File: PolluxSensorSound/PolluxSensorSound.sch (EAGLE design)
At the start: 5 parts

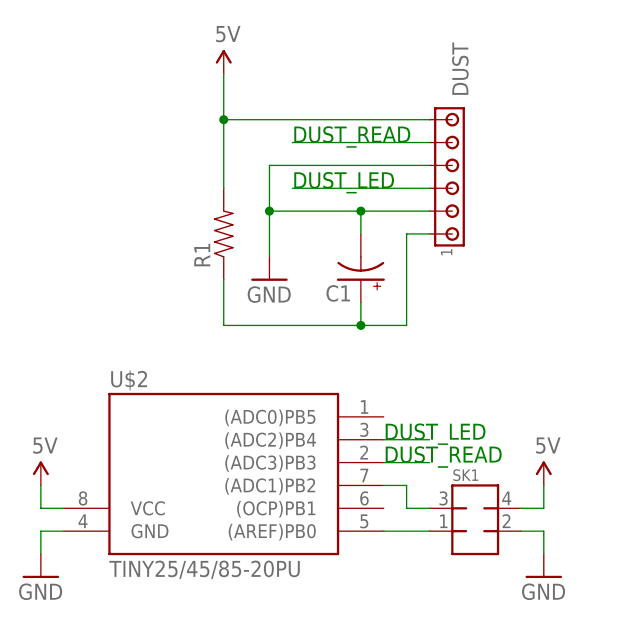
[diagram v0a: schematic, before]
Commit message: add SPL sensor board and schematics
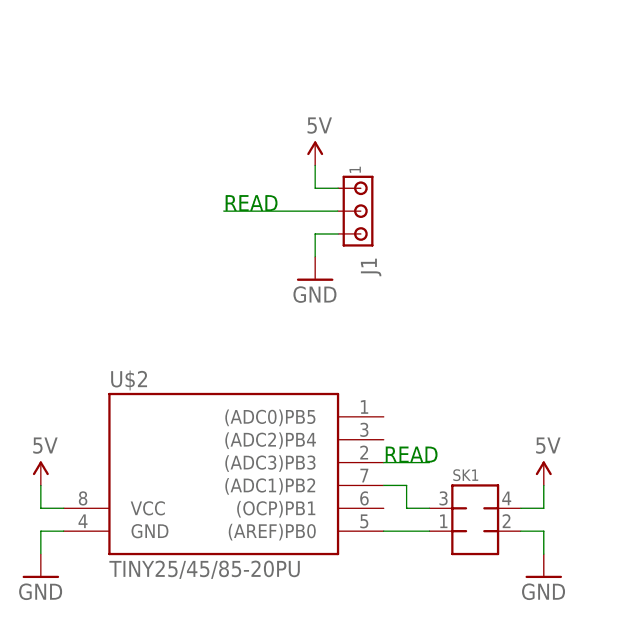
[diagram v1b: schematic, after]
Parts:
- removed C1: (no value), SparkFun:CAP_POLPTH4
- removed DUST: (no value), con-amp:MTA06-100
- removed R1: (no value), SparkFun:RESISTORAXIAL-0.3
- added J1: (no value), con-amp:MTA03-100
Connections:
- removed net DUST_LED: DUST.3, U$2.(ADC2)PB4
- removed net DUST_READ: DUST.5, U$2.(ADC3)PB3
- removed net N$4: C1.+, DUST.1, R1.1
- new net READ: J1.2, U$2.(ADC3)PB3
- net 5V: now also J1.1; no longer DUST.6, R1.2
- net GND: now also J1.3; no longer C1.-, DUST.2, DUST.4
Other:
- note added: "READ"
- note removed: "DUST_LED"
- note removed: "DUST_READ"
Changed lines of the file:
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@@
 <part name="SK1" library="jt-con-micromatch" deviceset="MMATCH-8-*" device="PTH"/>
 <part name="U$2" library="avr-7" deviceset="TINY25/45/85" device="-20PU"/>
-<part name="C1" library="SparkFun" deviceset="CAP_POL" device="PTH4"/>
-<part name="R1" library="SparkFun" deviceset="RESISTOR" device="AXIAL-0.3"/>
-<part name="DUST" library="con-amp" deviceset="MTA06-100" device=""/>
 <part name="U$3" library="SparkFun" deviceset="5V" device=""/>
 <part name="U$4" library="SparkFun" deviceset="5V" device=""/>
 <part name="GND2" library="SparkFun" deviceset="GND" device=""/>
 <part name="GND3" library="SparkFun" deviceset="GND" device=""/>
+<part name="J1" library="con-amp" deviceset="MTA03-100" device=""/>
 </parts>
 <sheets>
 <sheet>
 <plain>
-<text x="71.12" y="30.48" size="1.778" layer="91">DUST_READ</text>
-<text x="71.12" y="33.02" size="1.778" layer="91">DUST_LED</text>
-<text x="60.96" y="60.96" size="1.778" layer="91">DUST_LED</text>
-<text x="60.96" y="66.04" size="1.778" layer="91">DUST_READ</text>
+<text x="71.12" y="30.48" size="1.778" layer="91">READ</text>
+<text x="53.34" y="58.42" size="1.778" layer="91">READ</text>
 </plain>
 <instances>
-<instance part="U$1" gate="G$1" x="53.34" y="73.66"/>
+<instance part="U$1" gate="G$1" x="63.5" y="63.5"/>
 <instance part="GND1" gate="1" x="88.9" y="17.78"/>
 <instance part="SK1" gate="G$1" x="81.28" y="22.86"/>
 <instance part="U$2" gate="G$1" x="53.34" y="27.94"/>
-<instance part="C1" gate="G$1" x="68.58" y="50.8" rot="R180"/>
-<instance part="R1" gate="G$1" x="53.34" y="55.88" rot="R90"/>
-<instance part="DUST" gate="G$1" x="78.74" y="60.96" rot="MR90"/>
 <instance part="U$3" gate="G$1" x="33.02" y="27.94"/>
 <instance part="U$4" gate="G$1" x="88.9" y="27.94"/>
 <instance part="GND2" gate="1" x="33.02" y="17.78"/>
-<instance part="GND3" gate="1" x="58.42" y="50.8"/>
+<instance part="GND3" gate="1" x="63.5" y="50.8"/>
+<instance part="J1" gate="G$1" x="68.58" y="58.42" rot="R270"/>
 </instances>
 <busses>
@@
 </segment>
 <segment>
-<pinref part="R1" gate="G$1" pin="2"/>
+<pinref part="J1" gate="G$1" pin="1"/>
 <pinref part="U$1" gate="G$1" pin="5V"/>
-<wire x1="53.34" y1="60.96" x2="53.34" y2="68.58" width="0.1524" layer="91"/>
-<wire x1="53.34" y1="68.58" x2="53.34" y2="73.66" width="0.1524" layer="91"/>
-<wire x1="53.34" y1="68.58" x2="76.2" y2="68.58" width="0.1524" layer="91"/>
-<pinref part="DUST" gate="G$1" pin="6"/>
-<junction x="53.34" y="68.58"/>
-</segment>
-</net>
-<net name="DUST_LED" class="0">
-<segment>
-<pinref part="DUST" gate="G$1" pin="3"/>
-<wire x1="76.2" y1="60.96" x2="60.96" y2="60.96" width="0.1524" layer="91"/>
-</segment>
-<segment>
-<pinref part="U$2" gate="G$1" pin="(ADC2)PB4"/>
-<wire x1="71.12" y1="33.02" x2="76.2" y2="33.02" width="0.1524" layer="91"/>
+<wire x1="66.04" y1="60.96" x2="63.5" y2="60.96" width="0.1524" layer="91"/>
+<wire x1="63.5" y1="60.96" x2="63.5" y2="63.5" width="0.1524" layer="91"/>
 </segment>
 </net>
@@
 <segment>
 <pinref part="GND3" gate="1" pin="GND"/>
-<wire x1="58.42" y1="53.34" x2="58.42" y2="58.42" width="0.1524" layer="91"/>
-<pinref part="DUST" gate="G$1" pin="2"/>
-<wire x1="76.2" y1="58.42" x2="68.58" y2="58.42" width="0.1524" layer="91"/>
-<pinref part="C1" gate="G$1" pin="-"/>
-<wire x1="68.58" y1="58.42" x2="68.58" y2="55.88" width="0.1524" layer="91"/>
-<wire x1="58.42" y1="58.42" x2="68.58" y2="58.42" width="0.1524" layer="91"/>
-<wire x1="58.42" y1="58.42" x2="58.42" y2="63.5" width="0.1524" layer="91"/>
-<pinref part="DUST" gate="G$1" pin="4"/>
-<wire x1="58.42" y1="63.5" x2="76.2" y2="63.5" width="0.1524" layer="91"/>
-<junction x="58.42" y="58.42"/>
-<junction x="68.58" y="58.42"/>
+<wire x1="63.5" y1="53.34" x2="63.5" y2="55.88" width="0.1524" layer="91"/>
+<pinref part="J1" gate="G$1" pin="3"/>
+<wire x1="63.5" y1="55.88" x2="66.04" y2="55.88" width="0.1524" layer="91"/>
 </segment>
 </net>
@@
 </segment>
 </net>
-<net name="DUST_READ" class="0">
+<net name="READ" class="0">
 <segment>
-<pinref part="DUST" gate="G$1" pin="5"/>
-<wire x1="76.2" y1="66.04" x2="60.96" y2="66.04" width="0.1524" layer="91"/>
+<pinref part="J1" gate="G$1" pin="2"/>
+<wire x1="66.04" y1="58.42" x2="53.34" y2="58.42" width="0.1524" layer="91"/>
 </segment>
 <segment>
@@
 </segment>
 </net>
-<net name="N$4" class="0">
-<segment>
-<pinref part="R1" gate="G$1" pin="1"/>
-<wire x1="53.34" y1="50.8" x2="53.34" y2="45.72" width="0.1524" layer="91"/>
-<pinref part="DUST" gate="G$1" pin="1"/>
-<wire x1="76.2" y1="55.88" x2="73.66" y2="55.88" width="0.1524" layer="91"/>
-<wire x1="73.66" y1="55.88" x2="73.66" y2="45.72" width="0.1524" layer="91"/>
-<wire x1="73.66" y1="45.72" x2="68.58" y2="45.72" width="0.1524" layer="91"/>
-<pinref part="C1" gate="G$1" pin="+"/>
-<wire x1="68.58" y1="45.72" x2="53.34" y2="45.72" width="0.1524" layer="91"/>
-<wire x1="68.58" y1="48.26" x2="68.58" y2="45.72" width="0.1524" layer="91"/>
-<junction x="68.58" y="45.72"/>
-</segment>
-</net>

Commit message: improve sensor board
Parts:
- removed J1: (no value), con-amp:MTA03-100
- added C1: 1 uF, SparkFun:CAP_POLPTH2
- added SOUND: (no value), pinhead-2:PINHD-1X04_2.00
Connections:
- removed net N$2 (its old number): SK1.1, U$2.(AREF)PB0
- new net SDA: SK1.4, U$2.(AREF)PB0
- net 5V: now also C1.+, SK1.1, SOUND.3; no longer J1.1, SK1.4
- net GND: now also C1.-, SOUND.4; no longer J1.3
- net READ: now also SOUND.1; no longer J1.2
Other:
- note added: "SCL"
- note added: "SDA"
- moved on the sheet: SK1
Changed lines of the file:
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@@
 <layer number="56" name="wert" color="7" fill="1" visible="no" active="no"/>
 <layer number="91" name="Nets" color="2" fill="1" visible="yes" active="yes"/>
-<layer number="92" name="Busses" color="1" fill="1" visible="yes" active="yes"/>
+<layer number="92" name="Busses" color="1" fill="1" visible="no" active="yes"/>
 <layer number="93" name="Pins" color="2" fill="1" visible="no" active="yes"/>
 <layer number="94" name="Symbols" color="4" fill="1" visible="yes" active="yes"/>
@@
 <part name="GND2" library="SparkFun" deviceset="GND" device=""/>
 <part name="GND3" library="SparkFun" deviceset="GND" device=""/>
-<part name="J1" library="con-amp" deviceset="MTA03-100" device=""/>
+<part name="C1" library="SparkFun" deviceset="CAP_POL" device="PTH2" value="1 uF"/>
+<part name="U$5" library="SparkFun" deviceset="5V" device=""/>
+<part name="GND4" library="SparkFun" deviceset="GND" device=""/>
+<part name="SOUND" library="pinhead-2" deviceset="PINHD-1X04" device="_2.00"/>
 </parts>
 <sheets>
@@
 <plain>
 <text x="71.12" y="30.48" size="1.778" layer="91">READ</text>
-<text x="53.34" y="58.42" size="1.778" layer="91">READ</text>
+<text x="60.96" y="60.96" size="1.778" layer="91">READ</text>
+<text x="71.12" y="22.86" size="1.778" layer="91">SDA</text>
+<text x="91.44" y="27.94" size="1.778" layer="91">SDA</text>
+<text x="71.12" y="27.94" size="1.778" layer="91">SCL</text>
 </plain>
 <instances>
-<instance part="U$1" gate="G$1" x="63.5" y="63.5"/>
-<instance part="GND1" gate="1" x="88.9" y="17.78"/>
-<instance part="SK1" gate="G$1" x="81.28" y="22.86"/>
+<instance part="U$1" gate="G$1" x="68.58" y="63.5"/>
+<instance part="GND1" gate="1" x="93.98" y="20.32"/>
+<instance part="SK1" gate="G$1" x="86.36" y="25.4"/>
 <instance part="U$2" gate="G$1" x="53.34" y="27.94"/>
-<instance part="U$3" gate="G$1" x="33.02" y="27.94"/>
-<instance part="U$4" gate="G$1" x="88.9" y="27.94"/>
+<instance part="U$3" gate="G$1" x="33.02" y="38.1"/>
+<instance part="U$4" gate="G$1" x="78.74" y="35.56"/>
 <instance part="GND2" gate="1" x="33.02" y="17.78"/>
-<instance part="GND3" gate="1" x="63.5" y="50.8"/>
-<instance part="J1" gate="G$1" x="68.58" y="58.42" rot="R270"/>
+<instance part="GND3" gate="1" x="68.58" y="48.26"/>
+<instance part="C1" gate="G$1" x="86.36" y="58.42"/>
+<instance part="U$5" gate="G$1" x="86.36" y="63.5"/>
+<instance part="GND4" gate="1" x="86.36" y="48.26"/>
+<instance part="SOUND" gate="A" x="78.74" y="55.88"/>
 </instances>
 <busses>
 </busses>
 <nets>
-<net name="N$2" class="0">
-<segment>
-<pinref part="SK1" gate="G$1" pin="1"/>
-<pinref part="U$2" gate="G$1" pin="(AREF)PB0"/>
-<wire x1="76.2" y1="22.86" x2="71.12" y2="22.86" width="0.1524" layer="91"/>
-</segment>
-</net>
 <net name="5V" class="0">
-<segment>
-<pinref part="SK1" gate="G$1" pin="4"/>
-<wire x1="86.36" y1="25.4" x2="88.9" y2="25.4" width="0.1524" layer="91"/>
-<pinref part="U$4" gate="G$1" pin="5V"/>
-<wire x1="88.9" y1="25.4" x2="88.9" y2="27.94" width="0.1524" layer="91"/>
-</segment>
 <segment>
 <pinref part="U$2" gate="G$1" pin="VCC"/>
 <wire x1="35.56" y1="25.4" x2="33.02" y2="25.4" width="0.1524" layer="91"/>
 <pinref part="U$3" gate="G$1" pin="5V"/>
-<wire x1="33.02" y1="25.4" x2="33.02" y2="27.94" width="0.1524" layer="91"/>
+<wire x1="33.02" y1="25.4" x2="33.02" y2="38.1" width="0.1524" layer="91"/>
 </segment>
 <segment>
-<pinref part="J1" gate="G$1" pin="1"/>
 <pinref part="U$1" gate="G$1" pin="5V"/>
-<wire x1="66.04" y1="60.96" x2="63.5" y2="60.96" width="0.1524" layer="91"/>
-<wire x1="63.5" y1="60.96" x2="63.5" y2="63.5" width="0.1524" layer="91"/>
+<wire x1="68.58" y1="55.88" x2="68.58" y2="63.5" width="0.1524" layer="91"/>
+<pinref part="SOUND" gate="A" pin="3"/>
+<wire x1="76.2" y1="55.88" x2="68.58" y2="55.88" width="0.1524" layer="91"/>
+</segment>
+<segment>
+<pinref part="U$4" gate="G$1" pin="5V"/>
+<wire x1="78.74" y1="25.4" x2="78.74" y2="35.56" width="0.1524" layer="91"/>
+<pinref part="SK1" gate="G$1" pin="1"/>
+<wire x1="81.28" y1="25.4" x2="78.74" y2="25.4" width="0.1524" layer="91"/>
+</segment>
+<segment>
+<pinref part="C1" gate="G$1" pin="+"/>
+<pinref part="U$5" gate="G$1" pin="5V"/>
+<wire x1="86.36" y1="60.96" x2="86.36" y2="63.5" width="0.1524" layer="91"/>
 </segment>
 </net>
@@
 <segment>
 <pinref part="SK1" gate="G$1" pin="2"/>
-<wire x1="86.36" y1="22.86" x2="88.9" y2="22.86" width="0.1524" layer="91"/>
 <pinref part="GND1" gate="1" pin="GND"/>
-<wire x1="88.9" y1="22.86" x2="88.9" y2="20.32" width="0.1524" layer="91"/>
+<wire x1="91.44" y1="25.4" x2="93.98" y2="25.4" width="0.1524" layer="91"/>
+<wire x1="93.98" y1="25.4" x2="93.98" y2="22.86" width="0.1524" layer="91"/>
+</segment>
+<segment>
+<pinref part="C1" gate="G$1" pin="-"/>
+<pinref part="GND4" gate="1" pin="GND"/>
+<wire x1="86.36" y1="53.34" x2="86.36" y2="50.8" width="0.1524" layer="91"/>
 </segment>
 <segment>
 <pinref part="GND3" gate="1" pin="GND"/>
-<wire x1="63.5" y1="53.34" x2="63.5" y2="55.88" width="0.1524" layer="91"/>
-<pinref part="J1" gate="G$1" pin="3"/>
-<wire x1="63.5" y1="55.88" x2="66.04" y2="55.88" width="0.1524" layer="91"/>
-</segment>
-</net>
-<net name="N$1" class="0">
-<segment>
-<pinref part="U$2" gate="G$1" pin="(ADC1)PB2"/>
-<wire x1="71.12" y1="27.94" x2="73.66" y2="27.94" width="0.1524" layer="91"/>
-<wire x1="73.66" y1="27.94" x2="73.66" y2="25.4" width="0.1524" layer="91"/>
-<pinref part="SK1" gate="G$1" pin="3"/>
-<wire x1="73.66" y1="25.4" x2="76.2" y2="25.4" width="0.1524" layer="91"/>
+<wire x1="68.58" y1="50.8" x2="68.58" y2="53.34" width="0.1524" layer="91"/>
+<pinref part="SOUND" gate="A" pin="4"/>
+<wire x1="68.58" y1="53.34" x2="76.2" y2="53.34" width="0.1524" layer="91"/>
 </segment>
 </net>
 <net name="READ" class="0">
 <segment>
-<pinref part="J1" gate="G$1" pin="2"/>
-<wire x1="66.04" y1="58.42" x2="53.34" y2="58.42" width="0.1524" layer="91"/>
+<pinref part="SOUND" gate="A" pin="1"/>
+<wire x1="76.2" y1="60.96" x2="60.96" y2="60.96" width="0.1524" layer="91"/>
 </segment>
 <segment>
@@
 </segment>
 </net>
+<net name="N$2" class="0">
+<segment>
+<pinref part="U$2" gate="G$1" pin="(ADC1)PB2"/>
+<pinref part="SK1" gate="G$1" pin="3"/>
+<wire x1="71.12" y1="27.94" x2="81.28" y2="27.94" width="0.1524" layer="91"/>
+</segment>
+</net>
+<net name="SDA" class="0">
+<segment>
+<pinref part="U$2" gate="G$1" pin="(AREF)PB0"/>
+<wire x1="71.12" y1="22.86" x2="76.2" y2="22.86" width="0.1524" layer="91"/>
+</segment>
+<segment>
+<pinref part="SK1" gate="G$1" pin="4"/>
+<wire x1="91.44" y1="27.94" x2="96.52" y2="27.94" width="0.1524" layer="91"/>
+</segment>
+</net>
